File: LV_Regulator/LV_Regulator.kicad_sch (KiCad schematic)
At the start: 0 parts

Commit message: Folder structure added
Added a folder structure for documentation, code and component data; Added basic info to KiCad files
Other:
- company: (none) -> "Black Horntets" Formula Student team
- title: (none) -> LV_Regulator_Main
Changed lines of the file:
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@@
 	(generator_version "9.0")
 	(paper "A4")
+	(title_block
+		(title "LV_Regulator_Main")
+		(rev "1.00A")
+		(company "\"Black Horntets\" Formula Student team")
+		(comment 1 "Authors: Dusan Novkovic; Nikola Popovic")
+		(comment 2 "Subteam: Low Voltage Team")
+	)
 	(sheet_instances
 		(path "/"

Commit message: Added components
Added some basic isolation components to the LV_Regulator schematic.
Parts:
- added C1, C2: 100nF, symbol Device:C
- added C3, C5: 0.1uF, symbol Device:C
- added C4, C6: 10uF, symbol Device:C
- added IC1: UCC12040DVE, SOIC127P1030X265-16N, symbol UCC12040DVE:UCC12040DVE
- added K1: 41.52.9.005.0010, 415290050010, symbol 41.52.9.005.0010:41.52.9.005.0010
- added R1: 120, symbol Device:R
- added R2, R3: ---, symbol Device:R
- added U1: ADM2483xRW, Package_SO:SOIC-16W_7.5x10.3mm_P1.27mm, symbol Interface_UART:ADM2483xRW
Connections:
- new net: R1.1, R2.2, U1.13 (B)
- new net: R1.2, R3.1, U1.12 (A)
- new net +3V3: C2.1, U1.1 (VDD1), U1.7 (PV)
- new net +5V: C5.1, C6.1, IC1.1 (EN), IC1.3 (VINP)
- new net +5V_ISO: C1.2, C3.1, C4.1, IC1.13 (SEL), IC1.14 (VISO), R3.2, U1.16 (VDD2)
- new net GND: C2.2, C5.2, C6.2, IC1.2 (GNDP), IC1.4 (SYNC), IC1.6 (NC_1), IC1.7 (NC_2), IC1.8 (NC_3), U1.2 (GND1), U1.8 (GND1)
- new net GND_ISO: C1.1, C3.2, C4.2, IC1.10 (NC_4), IC1.11 (NC_5), IC1.12 (NC_6), IC1.15 (GNDS_2), IC1.16 (GNDS_3), IC1.9 (GNDS_1), R2.1, U1.15 (GND2), U1.9 (GND2)
- new net RS485-DIR: U1.4 (~{RE}), U1.5 (DE)
- new net RS485-RX: U1.3 (RxD)
- new net RS485-TX: U1.6 (TxD)

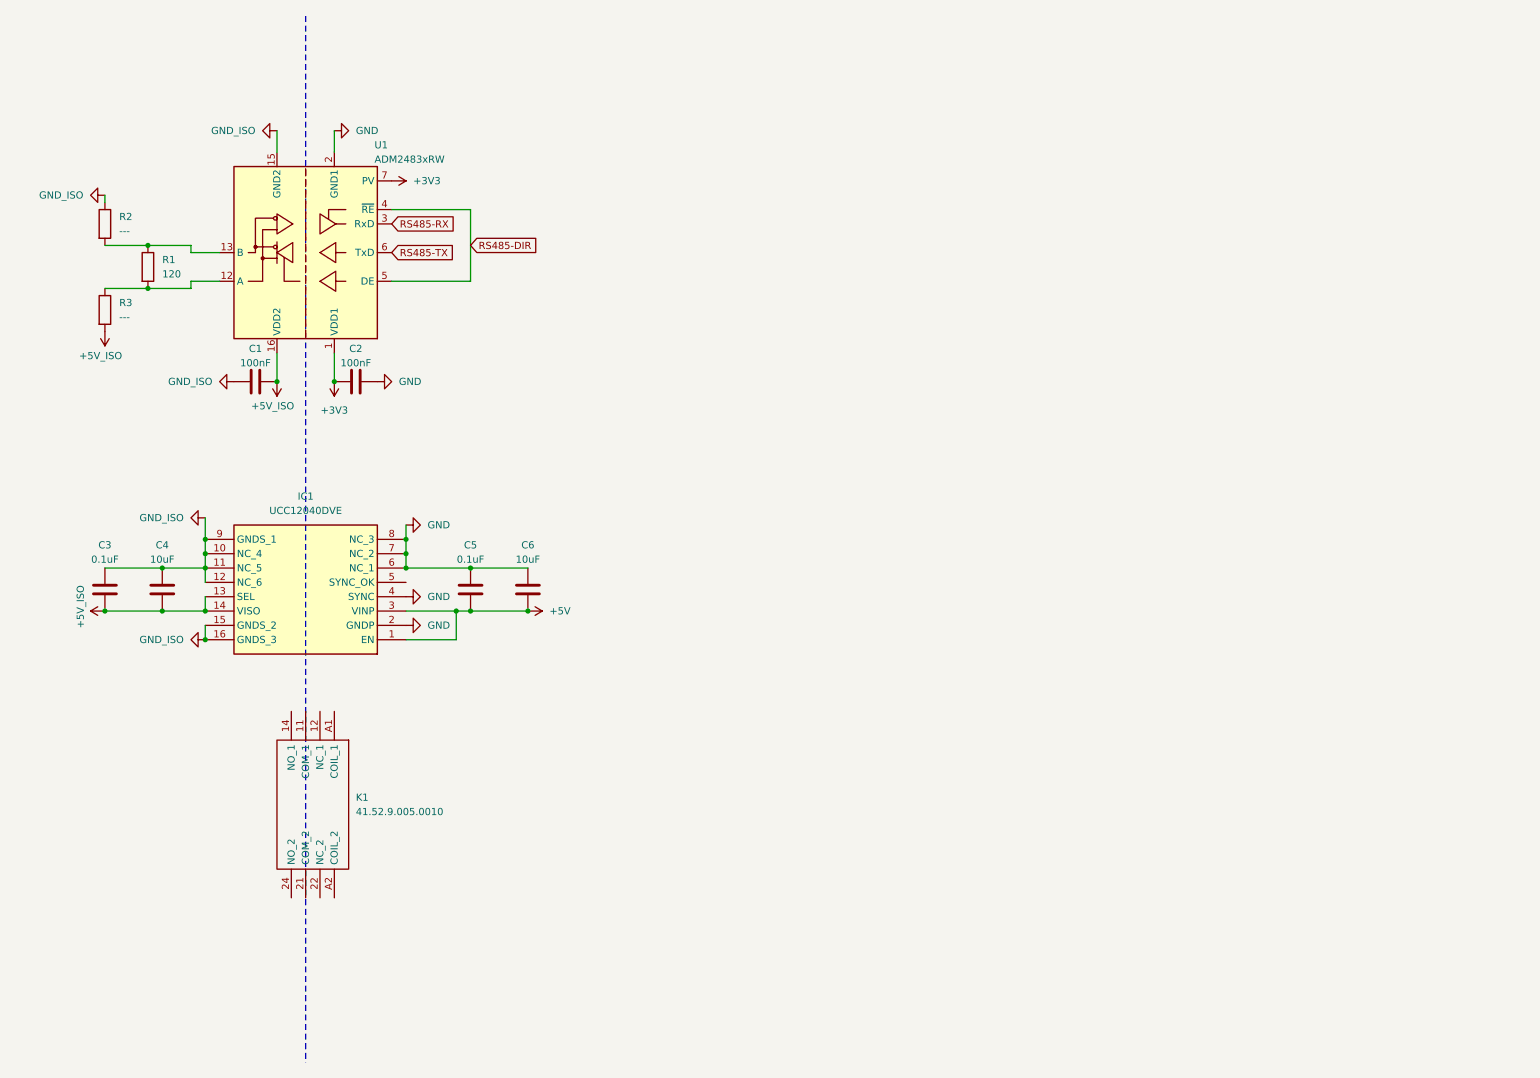
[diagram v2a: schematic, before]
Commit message: Modified LV_Regulator schematic; Added basic code configuration for LV_Reulator
Added the MCU to the schematic and some basic passives around it;
Added the basic STM32 program structure and set up the pin configuration to reflect the schematic.
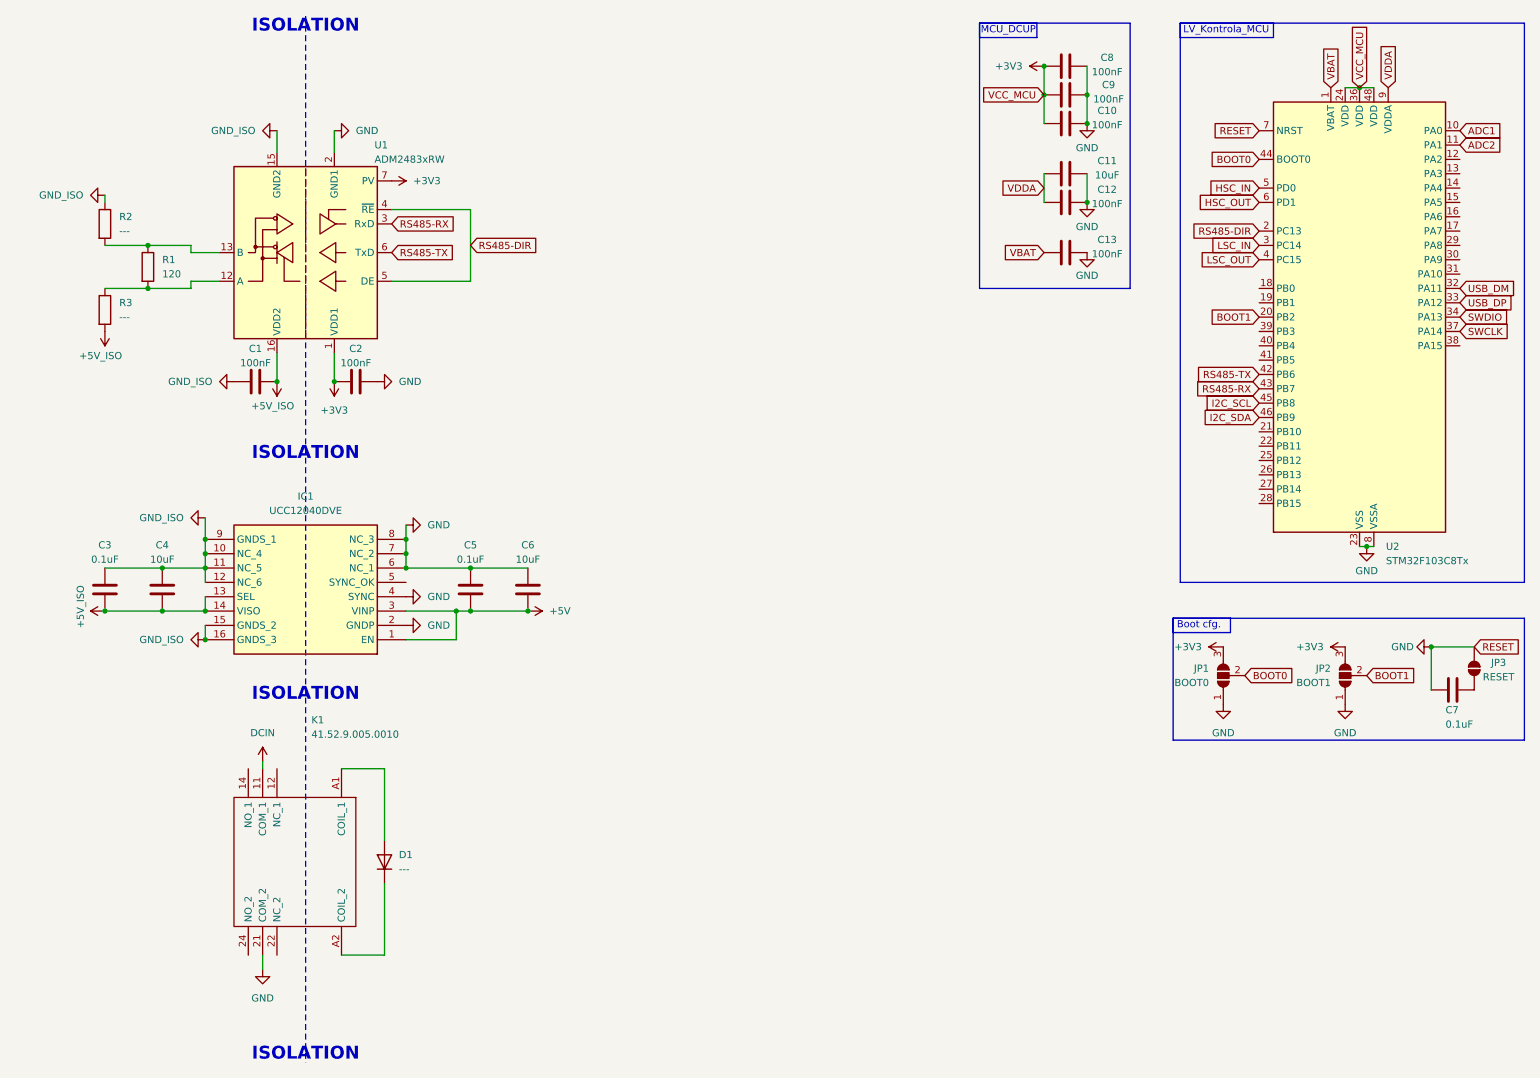
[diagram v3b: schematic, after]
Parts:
- added C10, C12, C13, C8, C9: 100nF, symbol Device:C
- added C11: 10uF, symbol Device:C
- added C7: 0.1uF, symbol Device:C
- added D1: ---, symbol Device:D
- added JP1: BOOT0, symbol Jumper:SolderJumper_3_Open
- added JP2: BOOT1, symbol Jumper:SolderJumper_3_Open
- added JP3: RESET, symbol Jumper:SolderJumper_2_Open
- added U2: STM32F103C8Tx, Package_QFP:LQFP-48_7x7mm_P0.5mm, symbol MCU_ST_STM32F1:STM32F103C8Tx
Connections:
- net +3V3: now also C10.1, C8.1, C9.1, JP1.3 (B), JP2.3 (B), U2.24 (VDD), U2.36 (VDD), U2.48 (VDD)
- net GND: now also K1.21 (COM_2), C10.2, C11.2, C12.2, C13.2, C7.2, C8.2, C9.2, JP1.1 (A), JP2.1 (A), JP3.1 (A), U2.23 (VSS), U2.35 (VSS), U2.47 (VSS), U2.7 (NRST), U2.8 (VSSA)
- net RS485-DIR: now also U2.2 (PC13)
- net RS485-RX: now also U2.43 (PB7)
- net RS485-TX: now also U2.42 (PB6)
- net DCIN: now reaches K1.11 (COM_1)
- net at K1.A1 (COIL_1): now also D1.2 (A)
- net at K1.A2 (COIL_2): now also D1.1 (K)
- new net: C7.1, JP3.2 (B)
- new net ADC1: U2.10 (PA0)
- new net ADC2: U2.11 (PA1)
- new net BOOT0: JP1.2 (C), U2.44 (BOOT0)
- new net BOOT1: JP2.2 (C), U2.20 (PB2)
- new net HSC_IN: U2.5 (PD0)
- new net HSC_OUT: U2.6 (PD1)
- new net I2C_SCL: U2.45 (PB8)
- new net I2C_SDA: U2.46 (PB9)
- new net LSC_IN: U2.3 (PC14)
- new net LSC_OUT: U2.4 (PC15)
- new net SWCLK: U2.37 (PA14)
- new net SWDIO: U2.34 (PA13)
- new net USB_DM: U2.32 (PA11)
- new net USB_DP: U2.33 (PA12)
- new net VBAT: C13.1, U2.1 (VBAT)
- new net VDDA: C11.1, C12.1, U2.9 (VDDA)
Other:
- note added: "Boot cfg."
- note added: "ISOLATION"
- note added: "LV_Kontrola_MCU"
- note added: "MCU_DCUP"

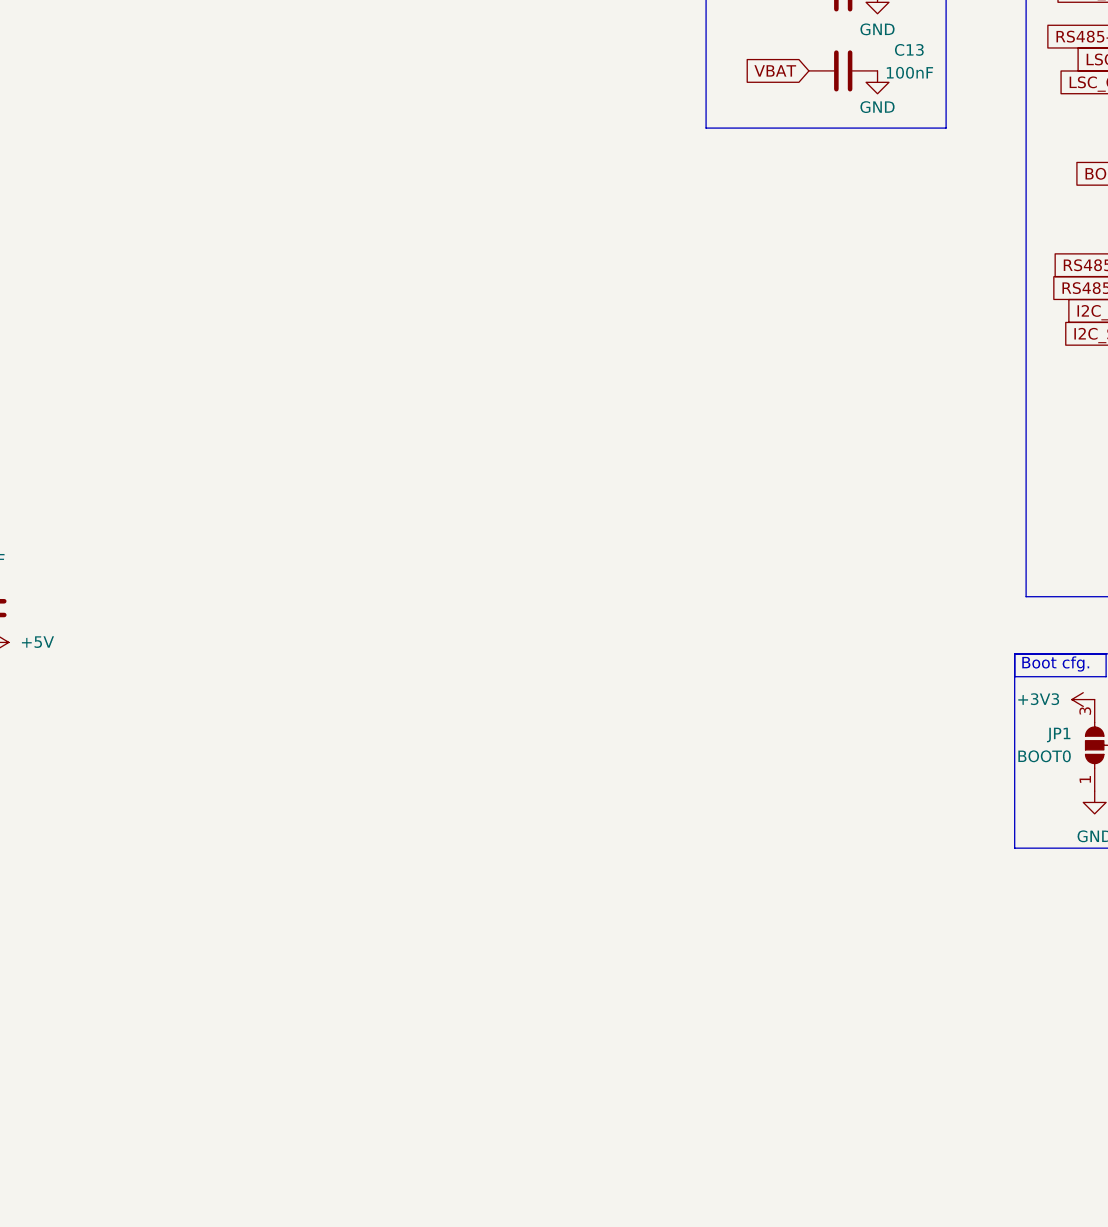
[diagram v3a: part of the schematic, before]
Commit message: Added LDOs
Added the two LDOs for 3v3 and 5v logic supply.
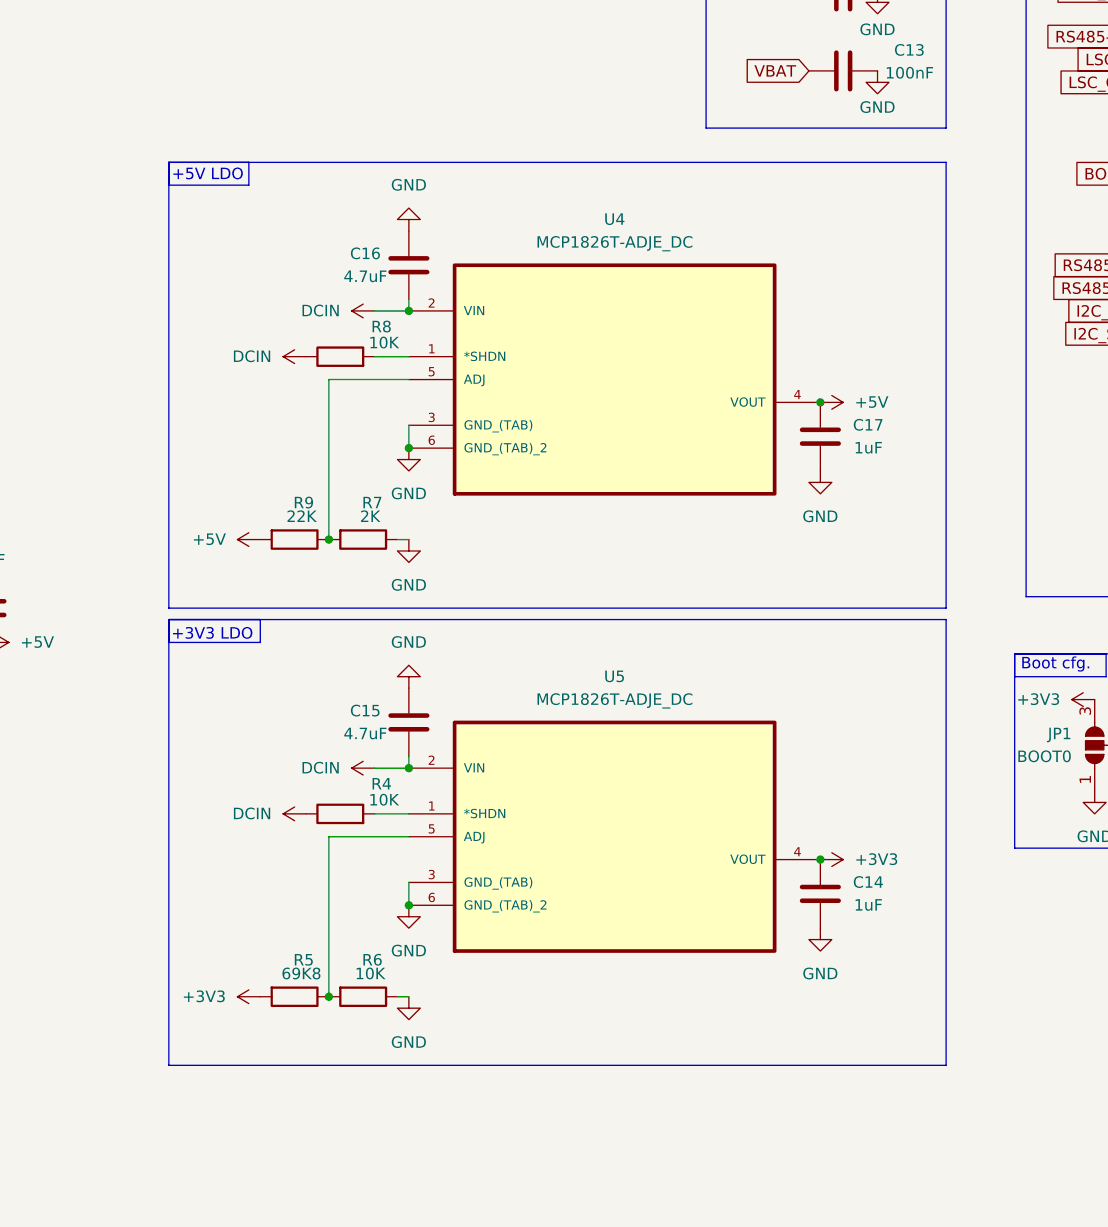
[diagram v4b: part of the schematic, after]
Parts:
- added C14, C17: 1uF, symbol Device:C
- added C15, C16: 4.7uF, symbol Device:C
- added R4, R6, R8: 10K, symbol Device:R
- added R5: 69K8, symbol Device:R
- added R7: 2K, symbol Device:R
- added R9: 22K, symbol Device:R
- added U4, U5: MCP1826T-ADJE_DC, MCP1826T-ADJE_DC:SOT230P700X180-6N, symbol MCP1826T-ADJE_DC:MCP1826T-ADJE_DC
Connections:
- net +3V3: now also C14.2, R6.2, U5.4 (VOUT)
- net +5V: now also C17.2, R7.2, U4.4 (VOUT)
- net DCIN: now also C15.2, C16.2, R4.1, R8.1, U4.2 (VIN), U5.2 (VIN)
- net GND: now also C14.1, C15.1, C16.1, C17.1, R5.1, R9.1, U4.3 (GND_(TAB)), U4.6 (GND_(TAB)_2), U5.3 (GND_(TAB)), U5.6 (GND_(TAB)_2)
- new net: R5.2, R6.1, U5.5 (ADJ)
- new net: R8.2, U4.1 (*SHDN)
- new net: R7.1, R9.2, U4.5 (ADJ)
- new net: R4.2, U5.1 (*SHDN)
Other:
- note added: "+3V3 LDO"
- note added: "+5V LDO"
